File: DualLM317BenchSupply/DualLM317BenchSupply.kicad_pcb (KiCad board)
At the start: 2 copper layers, 99.1 x 99.7 mm, 50 parts, among them CON101 BARREL_JACK, CON102 BARREL_JACK, P101 Vout+, P102 Vout-, SW101 SPDT, SW102 SPDT, SW103 SPDT, SW201 DP6T, U101 78L05, U102 LM317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

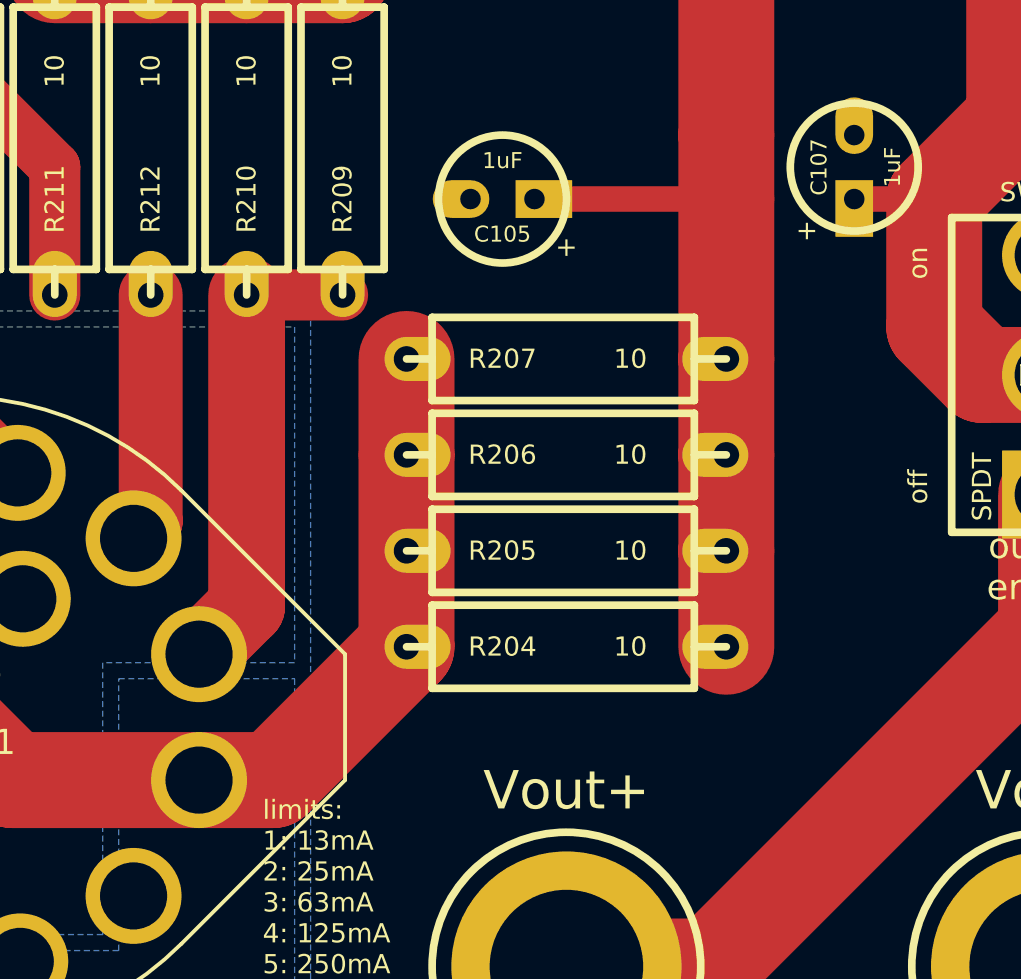
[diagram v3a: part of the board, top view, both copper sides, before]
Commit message: thinning traces for solderability
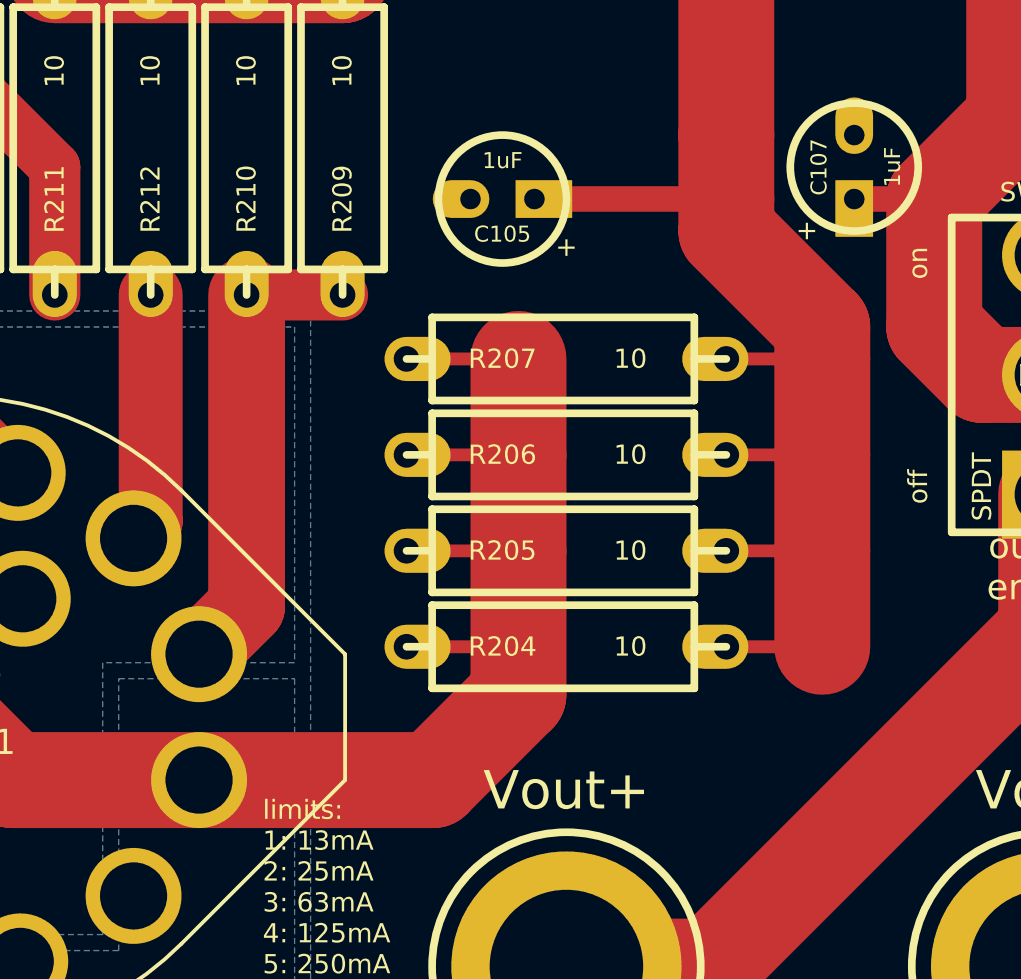
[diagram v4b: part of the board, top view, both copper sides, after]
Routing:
- net N-0000020: track 43.3 -> 68.6 mm
- net /current_limit_r/R_LIM-: track 183.6 -> 200.5 mm
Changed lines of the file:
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@@
   (general
     (links 86)
-    (no_connects 2)
+    (no_connects 1)
     (area 134.870999 113.280999 237.239001 216.284001)
     (thickness 1.6)
     (drawings 27)
-    (tracks 159)
+    (tracks 172)
     (zones 0)
     (modules 50)
@@
   (segment (start 139.7 170.18) (end 139.7 185.42) (width 3.81) (layer B.Cu) (net 1))
   (segment (start 172.4025 137.4775) (end 139.7 170.18) (width 3.81) (layer B.Cu) (net 1))
+  (segment (start 182.88 196.215) (end 186.69 196.215) (width 0.508) (layer F.Cu) (net 2) (status 400000))
+  (segment (start 186.69 196.215) (end 186.69 192.405) (width 3.81) (layer F.Cu) (net 2))
+  (segment (start 182.88 192.405) (end 186.69 192.405) (width 0.508) (layer F.Cu) (net 2) (status 400000))
+  (segment (start 182.88 188.595) (end 186.69 188.595) (width 0.508) (layer F.Cu) (net 2) (status 400000))
+  (segment (start 182.88 184.785) (end 186.69 184.785) (width 0.508) (layer F.Cu) (net 2) (status 400000))
+  (segment (start 182.88 178.435) (end 182.88 179.705) (width 3.81) (layer F.Cu) (net 2))
+  (segment (start 186.69 183.515) (end 186.69 184.785) (width 3.81) (layer F.Cu) (net 2))
+  (segment (start 186.69 184.785) (end 186.69 188.595) (width 3.81) (layer F.Cu) (net 2))
+  (segment (start 186.69 188.595) (end 186.69 192.405) (width 3.81) (layer F.Cu) (net 2))
+  (segment (start 182.88 179.705) (end 186.69 183.515) (width 3.81) (layer F.Cu) (net 2))
   (segment (start 189.865 133.985) (end 193.675 130.175) (width 0.508) (layer F.Cu) (net 2))
   (segment (start 199.39 130.81) (end 200.025 131.445) (width 0.508) (layer F.Cu) (net 2))
@@
   (segment (start 182.88 158.115) (end 182.88 175.895) (width 3.81) (layer F.Cu) (net 2))
   (segment (start 182.88 175.895) (end 182.88 178.435) (width 3.81) (layer F.Cu) (net 2))
-  (segment (start 182.88 178.435) (end 182.88 184.785) (width 3.81) (layer F.Cu) (net 2))
   (segment (start 146.05 172.085) (end 148.59 172.085) (width 1.524) (layer F.Cu) (net 2))
   (segment (start 143.51 172.085) (end 146.05 172.085) (width 1.016) (layer F.Cu) (net 2))
@@
   (segment (start 151.13 167.005) (end 153.67 167.005) (width 2.032) (layer F.Cu) (net 2))
   (segment (start 148.59 169.545) (end 151.13 167.005) (width 2.032) (layer F.Cu) (net 2))
-  (segment (start 182.88 196.215) (end 182.88 192.405) (width 3.81) (layer F.Cu) (net 2))
-  (segment (start 182.88 192.405) (end 182.88 188.595) (width 3.81) (layer F.Cu) (net 2))
-  (segment (start 182.88 188.595) (end 182.88 184.785) (width 3.81) (layer F.Cu) (net 2))
   (segment (start 167.64 169.545) (end 163.83 169.545) (width 3.81) (layer F.Cu) (net 2))
   (segment (start 163.83 169.545) (end 160.02 169.545) (width 3.81) (layer F.Cu) (net 2))
@@
   (segment (start 197.485 134.62) (end 195.58 136.525) (width 0.508) (layer F.Cu) (net 7))
   (segment (start 218.44 211.455) (end 221.615 211.455) (width 0.508) (layer F.Cu) (net 8))
-  (segment (start 154.305 143.51) (end 154.305 139.065) (width 0.508) (layer F.Cu) (net 9) (status 400000))
+  (segment (start 154.305 143.51) (end 154.305 139.065) (width 0.508) (layer F.Cu) (net 9))
   (segment (start 154.305 139.065) (end 153.035 139.065) (width 3.81) (layer F.Cu) (net 9))
   (segment (start 212.725 120.015) (end 210.82 120.015) (width 1.016) (layer F.Cu) (net 9))
@@
   (segment (start 161.94 196.51) (end 163.83 194.62) (width 3.048) (layer F.Cu) (net 10))
   (segment (start 163.83 194.62) (end 163.83 182.245) (width 3.048) (layer F.Cu) (net 10))
-  (segment (start 161.94 201.51) (end 164.885 201.51) (width 3.81) (layer F.Cu) (net 11))
-  (segment (start 164.885 201.51) (end 170.18 196.215) (width 3.81) (layer F.Cu) (net 11))
-  (segment (start 170.18 196.215) (end 170.18 188.595) (width 3.81) (layer F.Cu) (net 11))
-  (segment (start 170.18 188.595) (end 170.18 184.785) (width 3.81) (layer F.Cu) (net 11))
+  (segment (start 170.18 196.215) (end 174.625 196.215) (width 0.508) (layer F.Cu) (net 11) (status 400000))
+  (segment (start 174.625 196.215) (end 174.625 198.12) (width 0.508) (layer F.Cu) (net 11))
+  (segment (start 170.18 192.405) (end 174.625 192.405) (width 0.508) (layer F.Cu) (net 11) (status 400000))
+  (segment (start 170.18 188.595) (end 174.625 188.595) (width 0.508) (layer F.Cu) (net 11) (status 400000))
+  (segment (start 170.18 184.785) (end 174.625 184.785) (width 0.508) (layer F.Cu) (net 11) (status 400000))
+  (segment (start 171.235 201.51) (end 174.625 198.12) (width 3.81) (layer F.Cu) (net 11))
+  (segment (start 174.625 198.12) (end 174.625 198.12) (width 3.81) (layer F.Cu) (net 11))
+  (segment (start 174.625 198.12) (end 174.625 192.405) (width 3.81) (layer F.Cu) (net 11))
+  (segment (start 174.625 192.405) (end 174.625 188.595) (width 3.81) (layer F.Cu) (net 11))
+  (segment (start 174.625 188.595) (end 174.625 184.785) (width 3.81) (layer F.Cu) (net 11))
+  (segment (start 171.235 201.51) (end 161.94 201.51) (width 3.81) (layer F.Cu) (net 11) (status 800000))
   (segment (start 161.94 201.51) (end 154.52 201.51) (width 3.81) (layer F.Cu) (net 11))
   (segment (start 154.52 201.51) (end 149.52 196.51) (width 3.81) (layer F.Cu) (net 11))

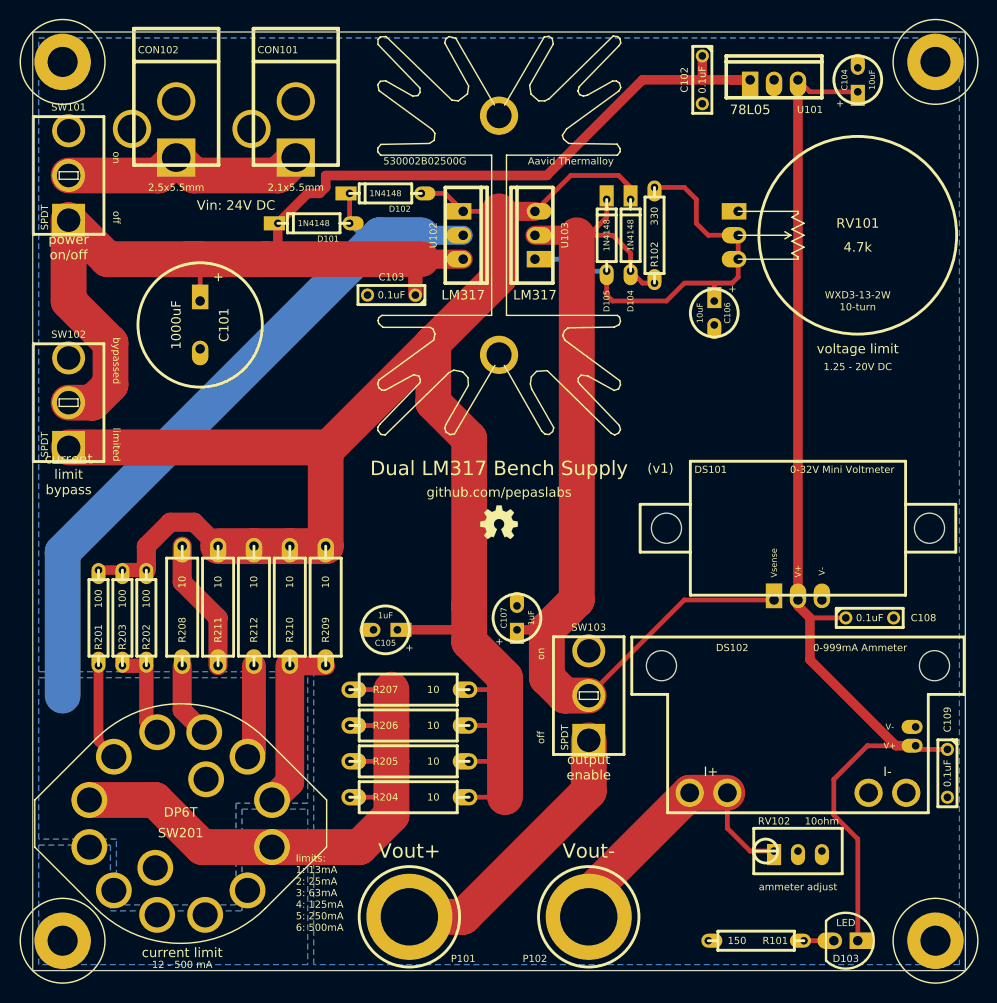
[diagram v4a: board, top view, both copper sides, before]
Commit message: thinning out traces for solderability
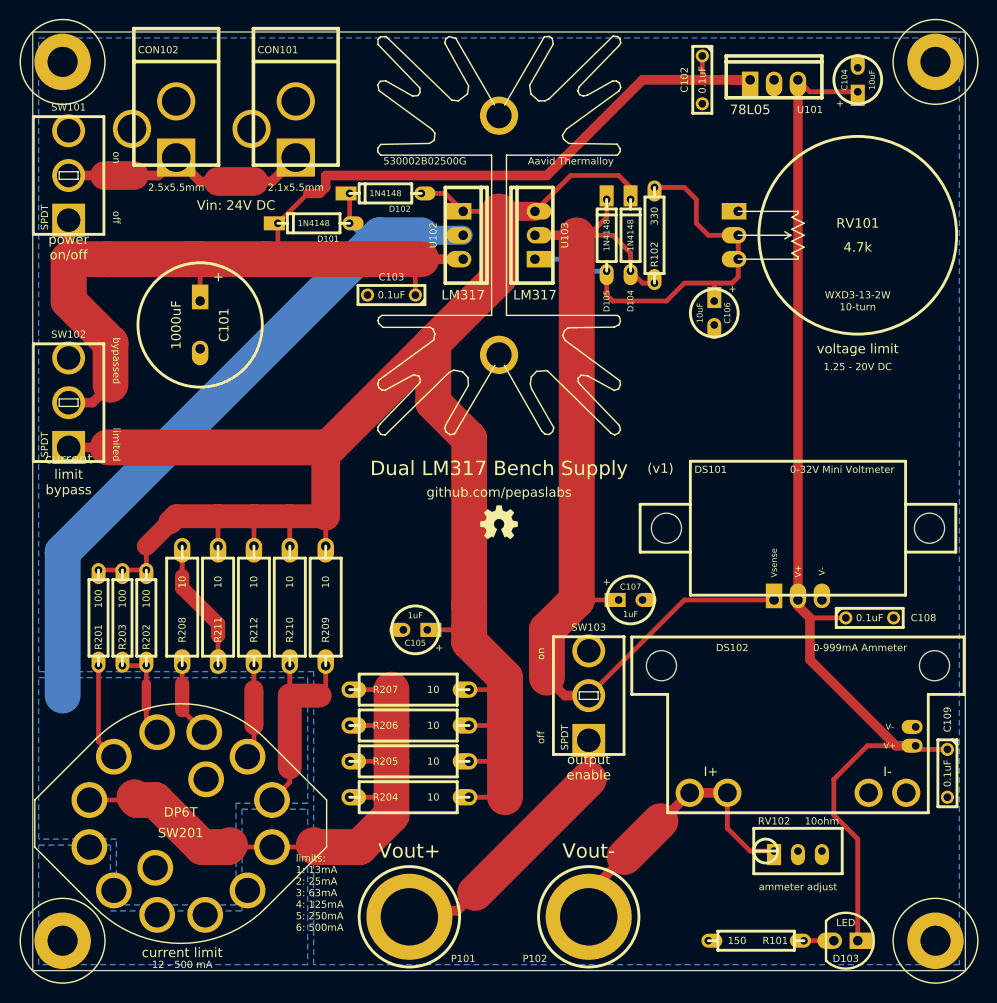
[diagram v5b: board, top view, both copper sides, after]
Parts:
- moved C107 11.3 mm to (198.8, 175.3), turned to 0 degrees
- moved C105 3.18 mm to (178.4, 178.4)
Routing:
- net /current_limit_r/R_LIM-: track 200.5 -> 205.7 mm
- net N-0000010: track 26.5 -> 29.7 mm
- net N-0000019: track 18.9 -> 21.7 mm
- net N-0000018: track 146.9 -> 145.2 mm
- net N-0000014: track 102.4 -> 103.7 mm
- net N-0000020: track 68.6 -> 69.6 mm
- net N-000005: track 30.0 -> 29.2 mm

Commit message: bumping board version.  more trace thinning.
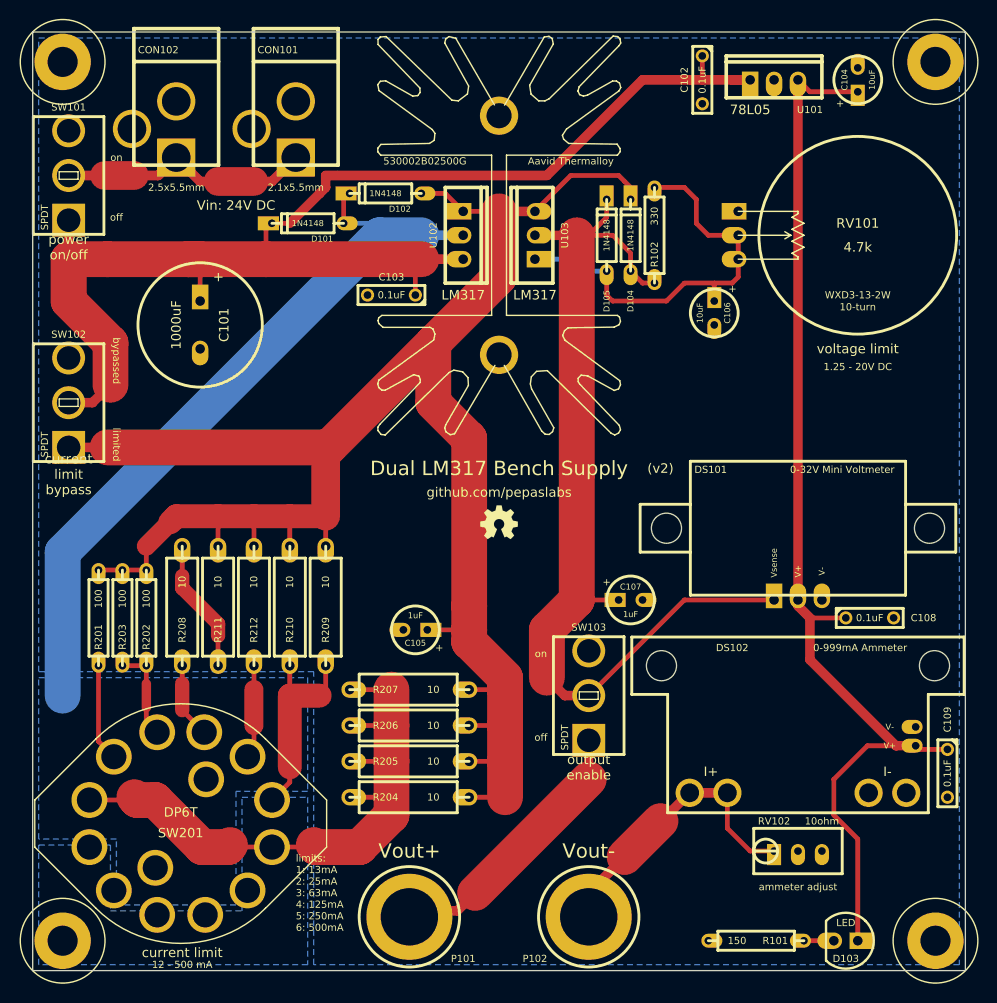
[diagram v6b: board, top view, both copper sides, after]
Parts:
- moved D101 0.64 mm to (169.5, 135.3)
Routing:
- net N-0000018: track 145.2 -> 147.3 mm
- net /current_limit_r/R_LIM+: track 78.0 -> 79.5 mm
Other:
- board text added: "(v2)"
- board text removed: "(v1)"

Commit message: updating gerbers
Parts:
- RV102: value 10ohm -> 10
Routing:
- net N-0000018: track 147.3 -> 148.4 mm
- net N-0000010: track 103.7 -> 104.3 mm

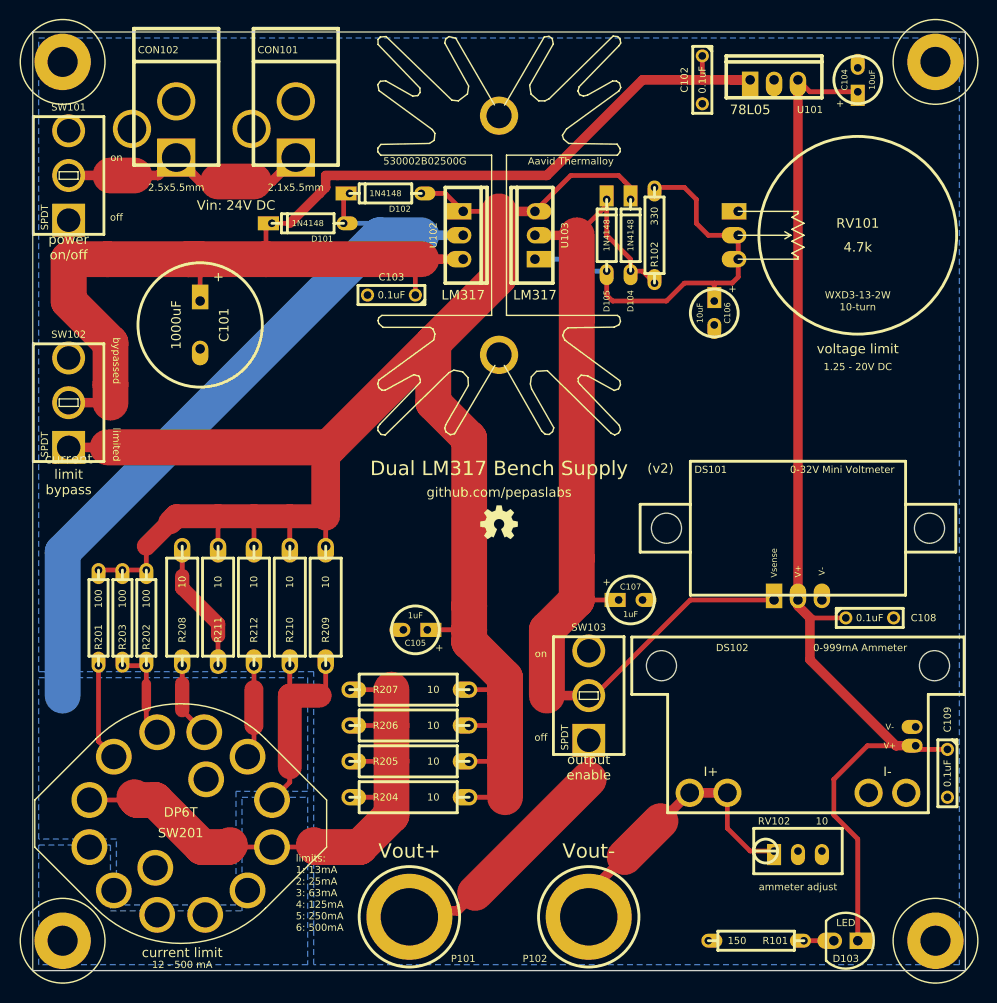
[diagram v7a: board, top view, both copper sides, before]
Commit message: adding 7812 before the 7805 to distribute the thermal load (a 7812 is cheaper than a heatsink :).
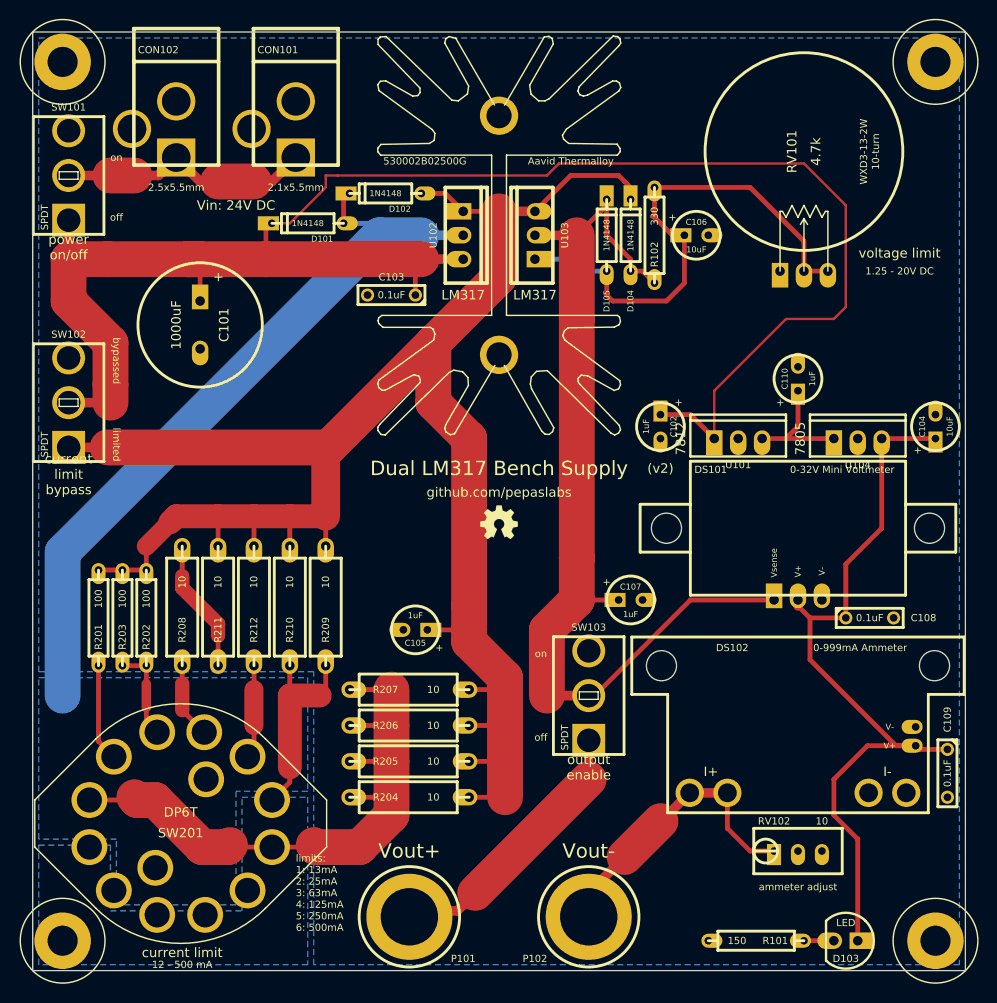
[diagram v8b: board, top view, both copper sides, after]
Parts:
- added C110: 1uF, ELCAP_10_20_V, F.Cu at (217.8, 153.0)
- added U104: 7805, TO-220_V_069B, F.Cu at (221.6, 158.1)
- C102: value 0.1uF -> 1uF; footprint C2 -> ELCAP_10_20_V
- U101: value 78L05 -> 7812
- moved U101 38.3 mm to (208.9, 158.1)
- moved C104 37.7 mm to (232.4, 158.1)
- moved C102 35.8 mm to (203.2, 155.6)
- moved RV101 10.6 mm to (218.4, 127.6), turned to 90 degrees
- moved C106 7.67 mm to (205.7, 136.5), turned to 0 degrees
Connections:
- U101 pad 3: 5V -> 12V
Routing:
- net N-0000018: track 148.4 -> 190.1 mm
- net 5V: track 119.7 -> 83.9 mm
- net 12V: track 0.00 -> 13.2 mm
- net N-000007: track 44.8 -> 56.2 mm
